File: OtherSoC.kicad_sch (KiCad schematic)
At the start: 1 part, among them U1 rv1126/rv1109

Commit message: fix some ERCs
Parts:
- U1: footprint (none) -> Rockchip_SoC:Rockchip_RV1126_FCCSP409LD_14.0x14.0mm
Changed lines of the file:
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@@
       (effects (font (size 1.27 1.27)))
     )
-    (property "Footprint" "" (at 104.14 156.21 0)
+    (property "Footprint" "Rockchip_SoC:Rockchip_RV1126_FCCSP409LD_14.0x14.0mm" (at 104.14 156.21 0)
       (effects (font (size 1.27 1.27)) hide)
     )
@@
     (pin "Y21")
     (pin "C21")
-    (pin "D20")
     (pin "D21")
     (pin "E19")
@@
       (effects (font (size 1.27 1.27)))
     )
-    (property "Footprint" "" (at 223.52 133.35 0)
+    (property "Footprint" "Rockchip_SoC:Rockchip_RV1126_FCCSP409LD_14.0x14.0mm" (at 223.52 133.35 0)
       (effects (font (size 1.27 1.27)) hide)
     )
@@
     (pin "Y21")
     (pin "C21")
-    (pin "D20")
     (pin "D21")
     (pin "E19")
@@
       (effects (font (size 1.27 1.27)))
     )
-    (property "Footprint" "" (at 99.06 73.66 0)
+    (property "Footprint" "Rockchip_SoC:Rockchip_RV1126_FCCSP409LD_14.0x14.0mm" (at 99.06 73.66 0)
       (effects (font (size 1.27 1.27)) hide)
     )
@@
     (pin "Y21")
     (pin "C21")
-    (pin "D20")
     (pin "D21")
     (pin "E19")
@@
       (effects (font (size 1.27 1.27)))
     )
-    (property "Footprint" "" (at 238.76 76.2 0)
+    (property "Footprint" "Rockchip_SoC:Rockchip_RV1126_FCCSP409LD_14.0x14.0mm" (at 238.76 76.2 0)
       (effects (font (size 1.27 1.27)) hide)
     )
@@
     (pin "Y21")
     (pin "C21")
-    (pin "D20")
     (pin "D21")
     (pin "E19")

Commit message: fix errors
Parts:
- added C?: 100nF X5R 6.3V, Capacitor_SMD:C_0201_0603Metric, symbol Device:C
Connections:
- net GND: now reaches U1.T8 (TVSS)
- net GND: now also C?.2
- net RESET: now reaches U1.W7 (nPOR_u)
- net RESET: now also C?.1
- no-connect marks 43 -> 41
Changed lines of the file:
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@@
 (kicad_sch (version 20230121) (generator eeschema)
   (paper "A4")
+  (junction (at 127 132.08) (diameter 0) (color 0 0 0 0)
+  )
   (no_connect (at 259.08 55.88))
-  (no_connect (at 93.98 128.27))
   (no_connect (at 214.63 101.6))
   (no_connect (at 259.08 38.1))
@@
   (no_connect (at 259.08 35.56))
   (no_connect (at 93.98 113.03))
-  (no_connect (at 93.98 132.08))
   (no_connect (at 259.08 43.18))
   (no_connect (at 259.08 48.26))
@@
   (no_connect (at 114.3 48.26))
   (no_connect (at 259.08 58.42))
+  (wire (pts (xy 93.98 128.27) (xy 109.22 128.27))
+    (stroke (width 0) (type default))
+  )
+  (wire (pts (xy 127 132.08) (xy 127 134.62))
+    (stroke (width 0) (type default))
+  )
+  (wire (pts (xy 93.98 132.08) (xy 127 132.08))
+    (stroke (width 0) (type default))
+  )
+  (wire (pts (xy 27.94 20.32) (xy 40.64 20.32))
+    (stroke (width 0) (type default))
+  )
+  (wire (pts (xy 127 132.08) (xy 128.27 132.08))
+    (stroke (width 0) (type default))
+  )
+  (wire (pts (xy 127 142.24) (xy 127 146.05))
+    (stroke (width 0) (type default))
+  )
+  (label "RESET" (at 128.27 132.08 0) (fields_autoplaced)
+    (effects (font (size 1.27 1.27)) (justify left bottom))
+  )
+  (label "RESET" (at 40.64 20.32 0) (fields_autoplaced)
+    (effects (font (size 1.27 1.27)) (justify left bottom))
+  )
+  (hierarchical_label "RESET" (shape input) (at 27.94 20.32 180) (fields_autoplaced)
+    (effects (font (size 1.27 1.27)) (justify right))
+  )
   (symbol (lib_id "CPU_Rockchip:rv1126_rv1109") (at 72.39 129.54 0) (unit 3)
     (in_bom yes) (on_board yes) (dnp no) (fields_autoplaced)
@@
     (pin "E20")
     (pin "F19")
-    (pin "F19")
     (pin "F20")
     (pin "F21")
@@
         (path "/e3b58043-16a3-43c8-9fad-9c9784eebfa4/56630686-fff3-4c34-8fc7-0dd6f7e78092"
           (reference "U1") (unit 3)
+        )
+      )
+    )
+  )
+  (symbol (lib_id "power:GND") (at 109.22 128.27 90) (unit 1)
+    (in_bom yes) (on_board yes) (dnp no) (fields_autoplaced)
+    (property "Reference" "#PWR?" (at 115.57 128.27 0)
+      (effects (font (size 1.27 1.27)) hide)
+    )
+    (property "Value" "GND" (at 112.395 128.5868 90)
+      (effects (font (size 1.27 1.27)) (justify right))
+    )
+    (property "Footprint" "" (at 109.22 128.27 0)
+      (effects (font (size 1.27 1.27)) hide)
+    )
+    (property "Datasheet" "" (at 109.22 128.27 0)
+      (effects (font (size 1.27 1.27)) hide)
+    )
+    (pin "1")
+    (instances
+      (project "leaf"
+        (path "/e3b58043-16a3-43c8-9fad-9c9784eebfa4/4417415c-26f1-4372-988d-9fdf1c116b4b"
+          (reference "#PWR?") (unit 1)
+        )
+        (path "/e3b58043-16a3-43c8-9fad-9c9784eebfa4/37e5f808-83b1-4839-b7a1-9684da8ab3e5"
+          (reference "#PWR033") (unit 1)
+        )
+        (path "/e3b58043-16a3-43c8-9fad-9c9784eebfa4/56630686-fff3-4c34-8fc7-0dd6f7e78092"
+          (reference "#PWR033") (unit 1)
+        )
+      )
+    )
+  )
+  (symbol (lib_id "power:GND") (at 127 146.05 0) (unit 1)
+    (in_bom yes) (on_board yes) (dnp no) (fields_autoplaced)
+    (property "Reference" "#PWR?" (at 127 152.4 0)
+      (effects (font (size 1.27 1.27)) hide)
+    )
+    (property "Value" "GND" (at 127 150.1855 0)
+      (effects (font (size 1.27 1.27)))
+    )
+    (property "Footprint" "" (at 127 146.05 0)
+      (effects (font (size 1.27 1.27)) hide)
+    )
+    (property "Datasheet" "" (at 127 146.05 0)
+      (effects (font (size 1.27 1.27)) hide)
+    )
+    (pin "1")
+    (instances
+      (project "leaf"
+        (path "/e3b58043-16a3-43c8-9fad-9c9784eebfa4/4417415c-26f1-4372-988d-9fdf1c116b4b"
+          (reference "#PWR?") (unit 1)
+        )
+        (path "/e3b58043-16a3-43c8-9fad-9c9784eebfa4/37e5f808-83b1-4839-b7a1-9684da8ab3e5"
+          (reference "#PWR034") (unit 1)
+        )
+        (path "/e3b58043-16a3-43c8-9fad-9c9784eebfa4/56630686-fff3-4c34-8fc7-0dd6f7e78092"
+          (reference "#PWR034") (unit 1)
         )
       )
@@
     (pin "E20")
     (pin "F19")
-    (pin "F19")
     (pin "F20")
     (pin "F21")
@@
     (pin "E20")
     (pin "F19")
-    (pin "F19")
     (pin "F20")
     (pin "F21")
@@
         (path "/e3b58043-16a3-43c8-9fad-9c9784eebfa4/56630686-fff3-4c34-8fc7-0dd6f7e78092"
           (reference "U1") (unit 8)
+        )
+      )
+    )
+  )
+  (symbol (lib_id "Device:C") (at 127 138.43 0) (unit 1)
+    (in_bom yes) (on_board yes) (dnp no)
+    (property "Reference" "C?" (at 128.27 137.16 90)
+      (effects (font (size 1.27 1.27)) (justify left))
+    )
+    (property "Value" "100nF X5R 6.3V" (at 123.19 148.59 90)
+      (effects (font (size 1.27 1.27)) (justify left))
+    )
+    (property "Footprint" "Capacitor_SMD:C_0201_0603Metric" (at 127.9652 142.24 0)
+      (effects (font (size 1.27 1.27)) hide)
+    )
+    (property "Datasheet" "~" (at 127 138.43 0)
+      (effects (font (size 1.27 1.27)) hide)
+    )
+    (property "Description" "容值: 100nF 精度: ±10% 额定电压: 6.3V 材质(温度系数): X5R 材质:X5R" (at 127 138.43 0)
+      (effects (font (size 1.27 1.27)) hide)
+    )
+    (property "LCSC" "C76928" (at 127 138.43 0)
+      (effects (font (size 1.27 1.27)) hide)
+    )
+    (property "Model" "GRM033R60J104KE19D" (at 127 138.43 0)
+      (effects (font (size 1.27 1.27)) hide)
+    )
+    (property "Vendor" "muRata(村田)" (at 127 138.43 0)
+      (effects (font (size 1.27 1.27)) hide)
+    )
+    (pin "1")
+    (pin "2")
+    (instances
+      (project "leaf"
+        (path "/e3b58043-16a3-43c8-9fad-9c9784eebfa4/9453ad46-b3ff-4d4e-8aa6-7cc75aa0f522/f6658df5-193a-49b6-ab60-4ac3c0bbbc45"
+          (reference "C?") (unit 1)
+        )
+        (path "/e3b58043-16a3-43c8-9fad-9c9784eebfa4/9453ad46-b3ff-4d4e-8aa6-7cc75aa0f522/f6658df5-193a-49b6-ab60-4ac3c0bbbc45/b7d33089-b835-4c65-840f-b2075d1befa5"
+          (reference "C?") (unit 1)
+        )
+        (path "/e3b58043-16a3-43c8-9fad-9c9784eebfa4/9453ad46-b3ff-4d4e-8aa6-7cc75aa0f522"
+          (reference "C?") (unit 1)
+        )
+        (path "/e3b58043-16a3-43c8-9fad-9c9784eebfa4/cc9fb3ac-19c3-47a8-ba7d-678b4d514ff0/8aa2eca1-edfe-4e9d-a854-96f51e82fbdb"
+          (reference "C?") (unit 1)
+        )
+        (path "/e3b58043-16a3-43c8-9fad-9c9784eebfa4/4417415c-26f1-4372-988d-9fdf1c116b4b"
+          (reference "C?") (unit 1)
+        )
+        (path "/e3b58043-16a3-43c8-9fad-9c9784eebfa4/37e5f808-83b1-4839-b7a1-9684da8ab3e5"
+          (reference "C26") (unit 1)
+        )
+        (path "/e3b58043-16a3-43c8-9fad-9c9784eebfa4/56630686-fff3-4c34-8fc7-0dd6f7e78092"
+          (reference "C26") (unit 1)
         )
       )
@@
     (pin "E20")
     (pin "F19")
-    (pin "F19")
     (pin "F20")

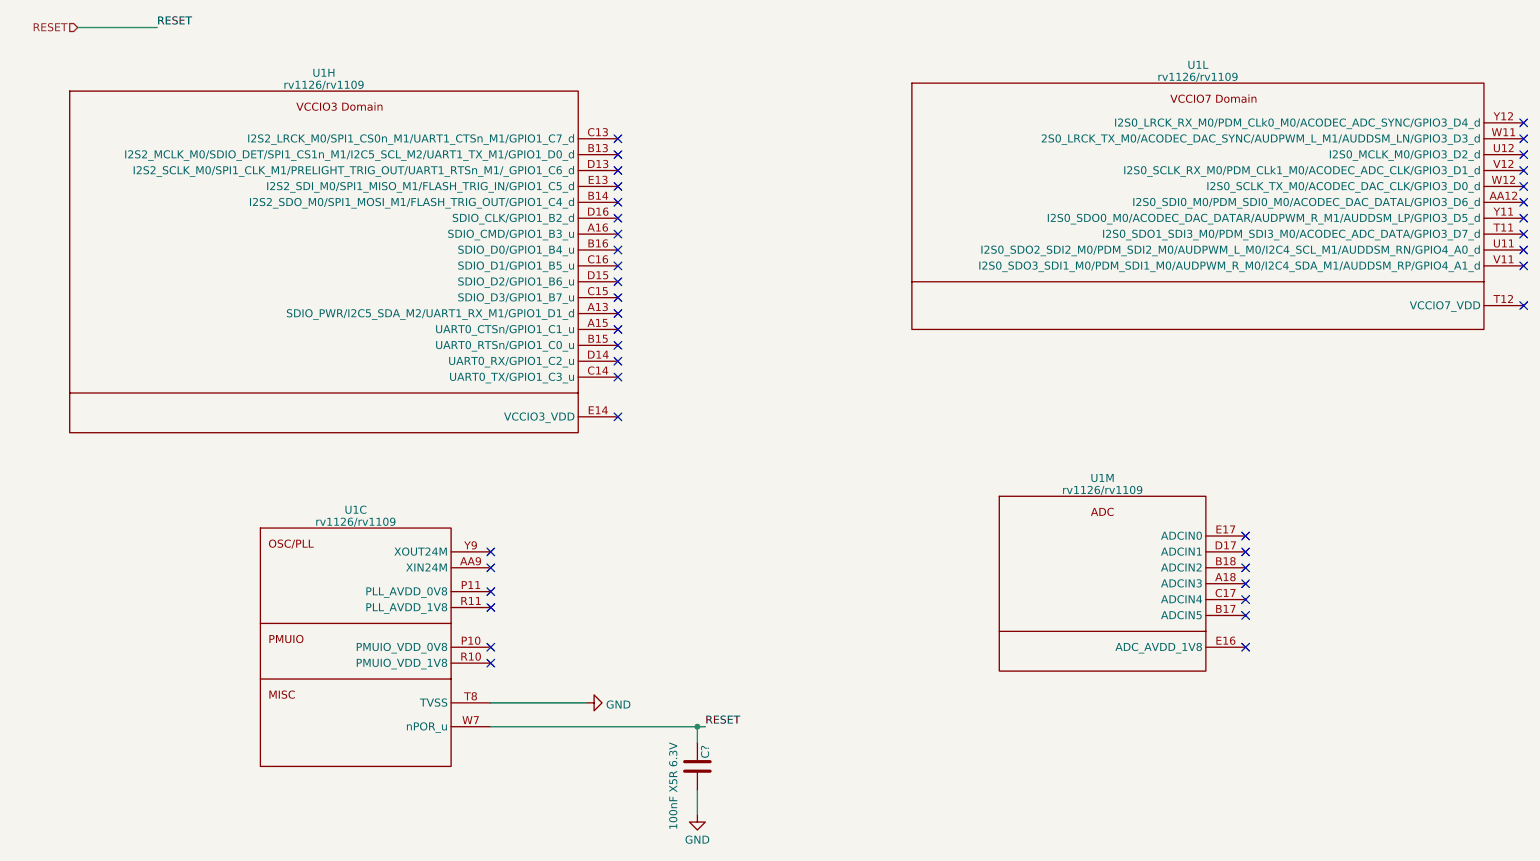
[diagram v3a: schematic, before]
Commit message: added OSC, updated annotations
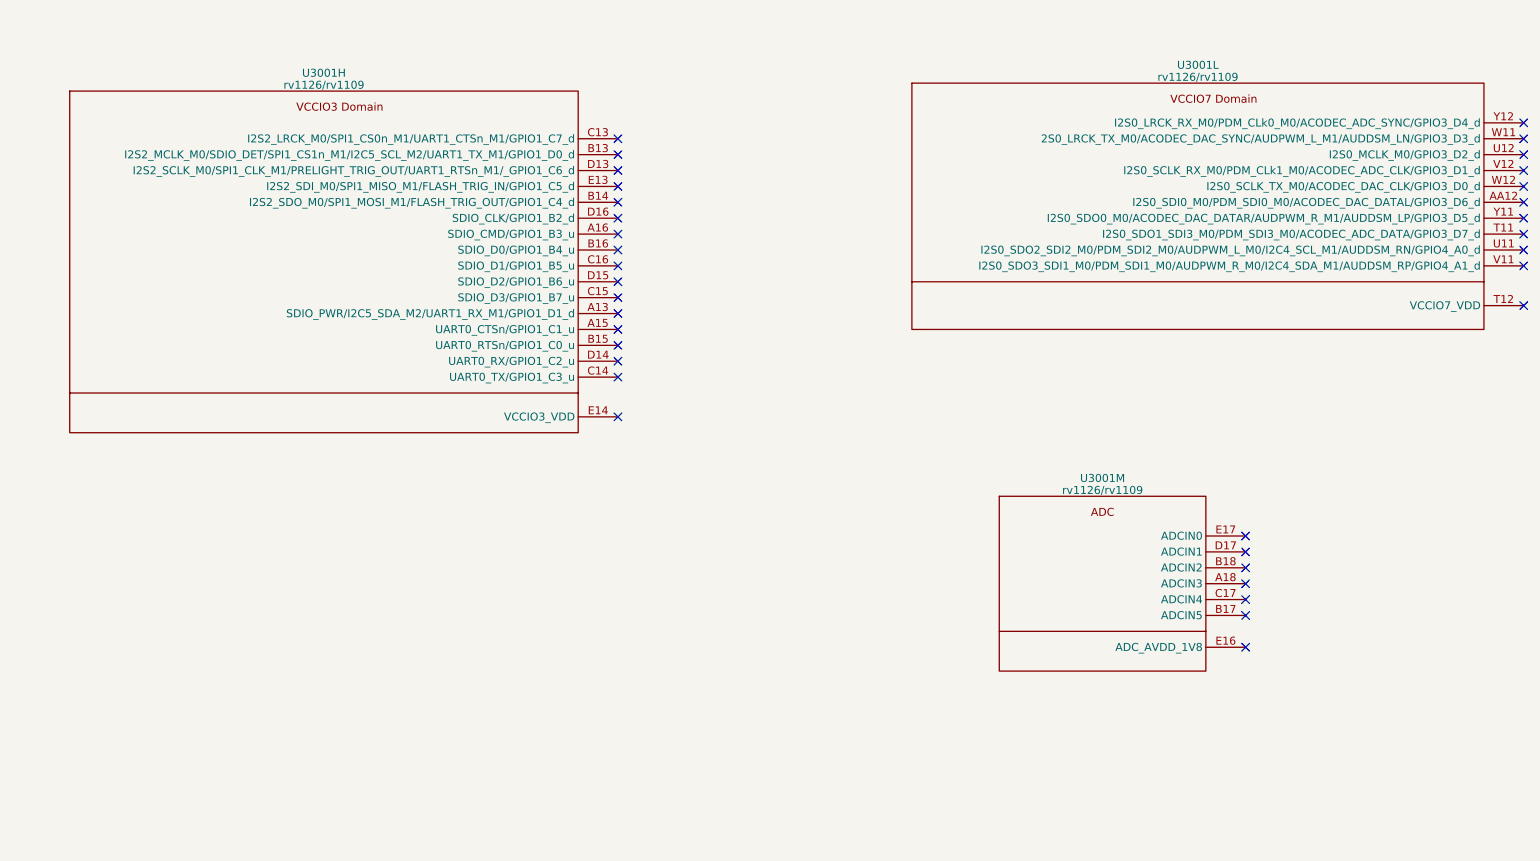
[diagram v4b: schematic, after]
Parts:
- removed C?: 100nF X5R 6.3V, Capacitor_SMD:C_0201_0603Metric, symbol Device:C
- removed unit 3 of U1
- renumbered U1 to U3001
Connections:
- no-connect marks 41 -> 35

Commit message: move DDR power decoupling capacitors into DDR4 Sheet
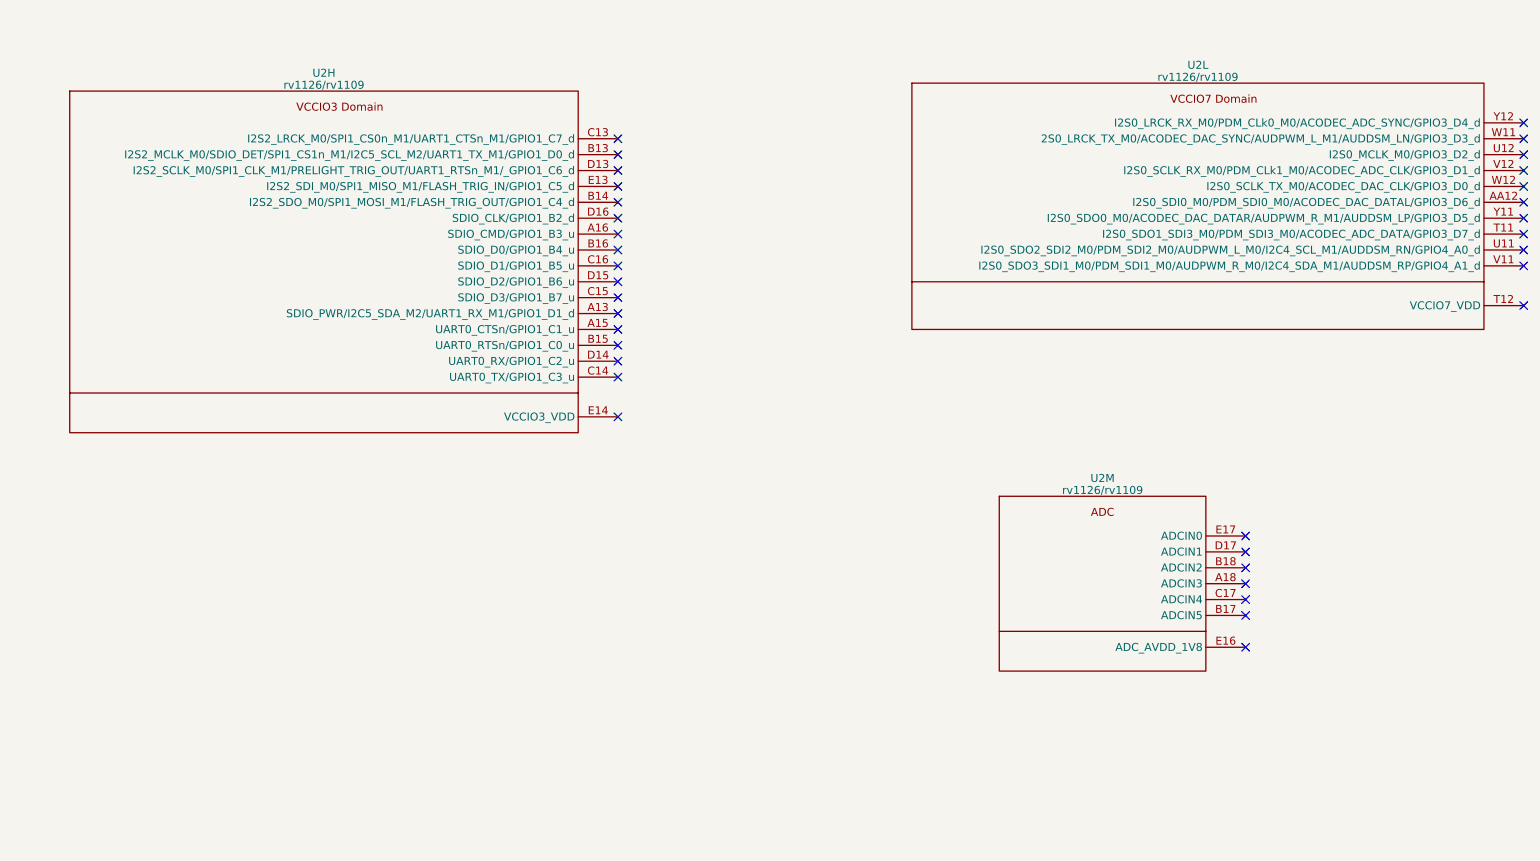
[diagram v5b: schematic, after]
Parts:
- renumbered U3001 to U2
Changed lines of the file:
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@@
   (symbol (lib_id "CPU_Rockchip:rv1126_rv1109") (at 191.77 106.68 0) (unit 13)
     (in_bom yes) (on_board yes) (dnp no) (fields_autoplaced)
-    (property "Reference" "U3001" (at 191.77 92.3671 0)
+    (property "Reference" "U2" (at 191.77 92.3671 0)
       (effects (font (size 1.27 1.27)))
     )
@@
       (project "leaf"
         (path "/e3b58043-16a3-43c8-9fad-9c9784eebfa4/56630686-fff3-4c34-8fc7-0dd6f7e78092"
-          (reference "U3001") (unit 13)
+          (reference "U2") (unit 13)
         )
       )
@@
   (symbol (lib_id "CPU_Rockchip:rv1126_rv1109") (at 67.31 46.99 0) (unit 8)
     (in_bom yes) (on_board yes) (dnp no) (fields_autoplaced)
-    (property "Reference" "U3001" (at 67.31 27.5971 0)
+    (property "Reference" "U2" (at 67.31 27.5971 0)
       (effects (font (size 1.27 1.27)))
     )
@@
       (project "leaf"
         (path "/e3b58043-16a3-43c8-9fad-9c9784eebfa4/56630686-fff3-4c34-8fc7-0dd6f7e78092"
-          (reference "U3001") (unit 8)
+          (reference "U2") (unit 8)
         )
       )
@@
   (symbol (lib_id "CPU_Rockchip:rv1126_rv1109") (at 207.01 49.53 0) (unit 12)
     (in_bom yes) (on_board yes) (dnp no) (fields_autoplaced)
-    (property "Reference" "U3001" (at 207.01 26.3271 0)
+    (property "Reference" "U2" (at 207.01 26.3271 0)
       (effects (font (size 1.27 1.27)))
     )
@@
       (project "leaf"
         (path "/e3b58043-16a3-43c8-9fad-9c9784eebfa4/56630686-fff3-4c34-8fc7-0dd6f7e78092"
-          (reference "U3001") (unit 12)
+          (reference "U2") (unit 12)
         )
       )

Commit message: added README and license
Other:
- company: (none) -> Yang Hongbo
- title: (none) -> Leaf RV1126
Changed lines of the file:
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@@
 (kicad_sch (version 20230121) (generator eeschema)
   (paper "A4")
+  (title_block
+    (title "Leaf RV1126")
+    (date "2023-06-07")
+    (company "Yang Hongbo")
+    (comment 1 "License: CC BY-SA")
+  )
   (no_connect (at 259.08 55.88))
   (no_connect (at 214.63 101.6))
